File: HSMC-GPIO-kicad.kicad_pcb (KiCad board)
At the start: 2 copper layers, 63.5 x 78.1 mm, 107 parts, among them J1 HSMC, J2 Conn_01x03_Male, J3 I2C, J4 Screw_Terminal_01x04, J5 Conn_02x20_Odd_Even, U1 MC78M05_TO252, U2 TCA9517

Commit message: Reroute GPIO pins (again)
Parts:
- C18, C19, C2, C20, C3: footprint Capacitor_Tantalum_SMD:CP_EIA-3528-21_Kemet-B -> Capacitor_Tantalum_SMD:CP_EIA-3528-15_AVX-H
- moved J2 76.4 mm to (8.87, 35.1)
- moved C5 76.4 mm to (9.00, 38.2)
- moved C6 76.4 mm to (3.67, 38.2)
- moved J3 76.4 mm to (13.1, 42.7)
- moved U2 76.4 mm to (6.97, 40.2)
- moved C2 38.8 mm to (9.41, 59.1)
- moved C3 38.8 mm to (7.40, 71.6)
- moved C4 38.8 mm to (11.6, 73.1)
- moved U1 38.8 mm to (11.3, 65.5)
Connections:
- J1 pad 102: /GPIO20 -> /GPIO19
- J1 pad 104: /GPIO21 -> /GPIO18
- J1 pad 108: /GPIO22 -> /GPIO17
- J1 pad 110: /GPIO23 -> /GPIO16
- J1 pad 114: /GPIO24 -> /GPIO15
- J1 pad 116: /GPIO25 -> /GPIO14
- J1 pad 120: /GPIO26 -> /GPIO13
- J1 pad 122: /GPIO27 -> /GPIO12
- J1 pad 126: /GPIO28 -> /GPIO11
- J1 pad 128: /GPIO29 -> /GPIO10
- J1 pad 132: /GPIO30 -> /GPIO9
- J1 pad 134: /GPIO31 -> /GPIO8
- J1 pad 138: /GPIO32 -> /GPIO7
- J1 pad 140: /GPIO33 -> /GPIO6
- J1 pad 144: /GPIO34 -> /GPIO5
- J1 pad 146: /GPIO35 -> /GPIO4
- J1 pad 150: /GPIO36 -> /GPIO3
- J1 pad 152: /GPIO37 -> /GPIO2
- J1 pad 156: /GPIO38 -> /GPIO1
- J1 pad 158: /GPIO39 -> /GPIO0
- J1 pad 42: /GPIO0 -> /GPIO39
- J1 pad 44: /GPIO1 -> /GPIO38
- J1 pad 48: /GPIO2 -> /GPIO37
- J1 pad 50: /GPIO3 -> /GPIO36
- J1 pad 54: /GPIO4 -> /GPIO35
- J1 pad 56: /GPIO5 -> /GPIO34
- J1 pad 60: /GPIO6 -> /GPIO33
- J1 pad 62: /GPIO7 -> /GPIO32
- J1 pad 66: /GPIO8 -> /GPIO31
- J1 pad 68: /GPIO9 -> /GPIO30
- J1 pad 72: /GPIO10 -> /GPIO29
- J1 pad 74: /GPIO11 -> /GPIO28
- J1 pad 78: /GPIO12 -> /GPIO27
- J1 pad 80: /GPIO13 -> /GPIO26
- J1 pad 84: /GPIO14 -> /GPIO25
- J1 pad 86: /GPIO15 -> /GPIO24
- J1 pad 90: /GPIO16 -> /GPIO23
- J1 pad 92: /GPIO17 -> /GPIO22
- J1 pad 96: /GPIO18 -> /GPIO21
- J1 pad 98: /GPIO19 -> /GPIO20
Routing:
- net +5V: track 120.8 -> 8.95 mm
- net +3V3: track 225.2 -> 146.9 mm
- net +12V: track 118.8 -> 68.6 mm
- net /SDA: track 38.3 -> 1.50 mm
- net /SCL: track 32.8 -> 1.50 mm
- net /GPIO0: track 40.3 -> 33.9 mm
- net /GPIO1: track 40.1 -> 33.7 mm
- net /GPIO2: track 40.5 -> 34.3 mm
- net /GPIO3: track 39.7 -> 34.1 mm
- net /GPIO38: track 34.9 -> 40.0 mm
- net /GPIO4: track 39.9 -> 34.8 mm
- net /GPIO39: track 34.7 -> 39.8 mm
- net /GPIO37: track 34.4 -> 39.4 mm
- net /GPIO5: track 39.3 -> 34.6 mm
- net /GPIO7: track 39.2 -> 35.0 mm
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
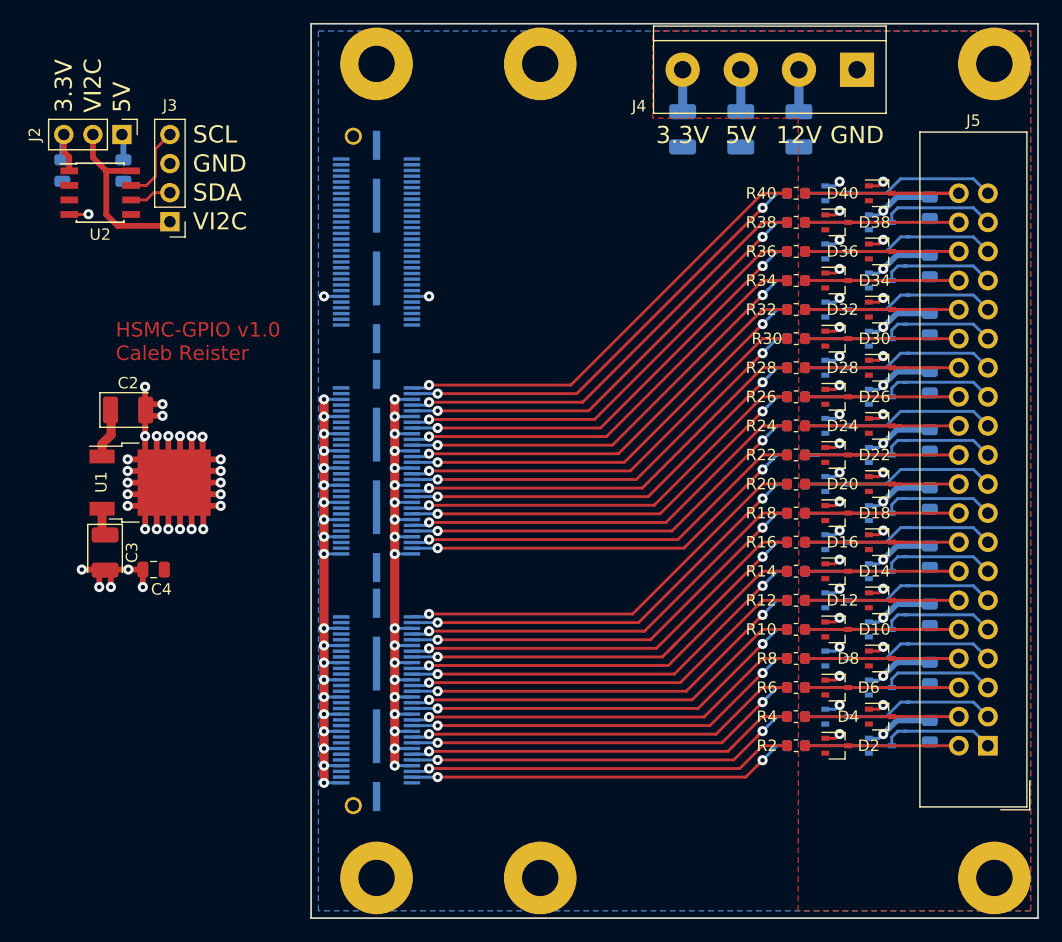
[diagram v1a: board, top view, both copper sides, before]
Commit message: Change BAT54S diode packages back to to SOT-23
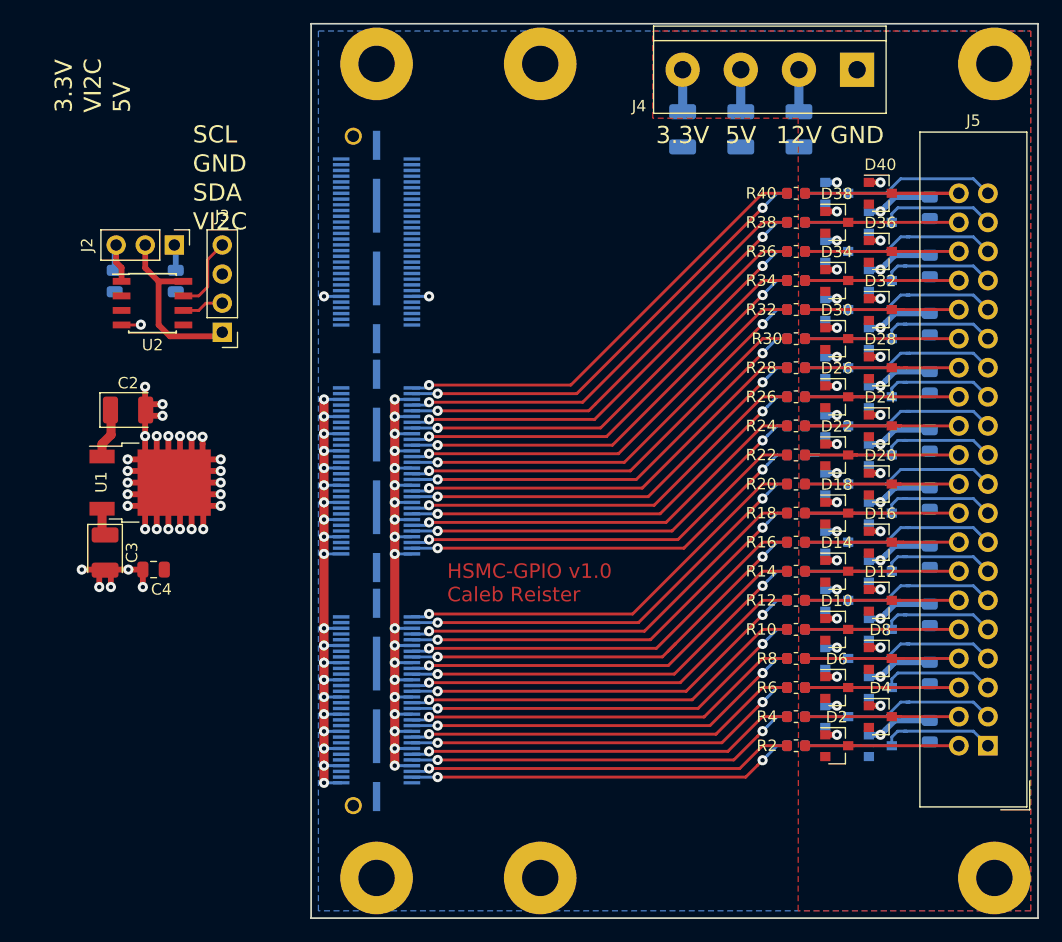
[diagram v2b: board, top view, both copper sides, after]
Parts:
- D1, D10, D11, D12, D13, D14, D15, D16, D17, D18, D19, D2, D20, D21, D22, D23, D24, D25, D26, D27, D28, D29, D3, D30, D31, D32, D33, D34, D35, D36, D37, D38, D39, D4, D40, D5, D6, D7, D8, D9: footprint Package_TO_SOT_SMD:SOT-323_SC-70 -> Package_TO_SOT_SMD:SOT-23
- moved C5 10.7 mm to (13.6, 47.9)
- moved C6 10.7 mm to (8.24, 47.9)
- moved J2 10.7 mm to (13.4, 44.7)
- moved J3 10.7 mm to (17.6, 52.3)
- moved U2 10.7 mm to (11.5, 49.8)
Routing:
- net GND: track 149.9 -> 142.1 mm
- net +3V3: track 146.9 -> 141.5 mm

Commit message: Fix issues and reroute I2C buffer, length match GPIO bus
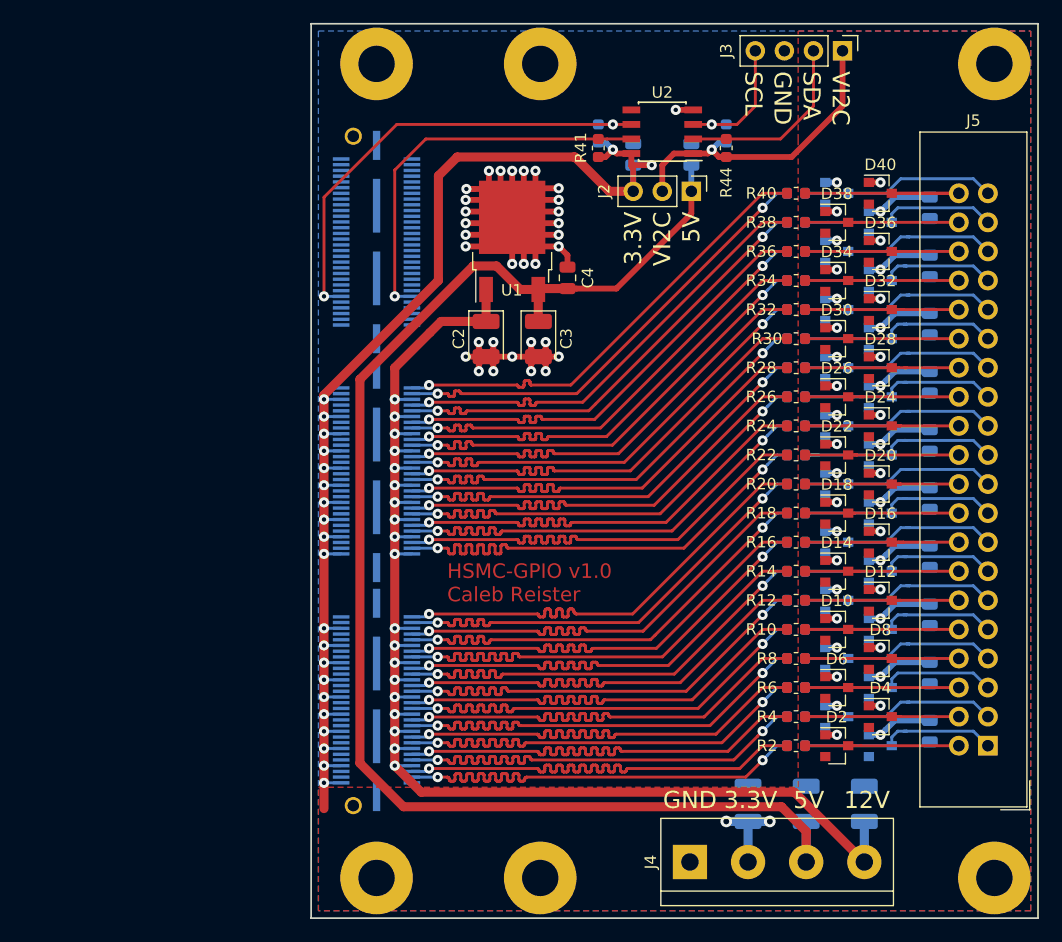
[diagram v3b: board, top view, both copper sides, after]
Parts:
- added R41: 10k, Resistor_SMD:R_0603_1608Metric, F.Cu at (50.5, 36.3)
- added R42: 10k, Resistor_SMD:R_0603_1608Metric, B.Cu at (50.5, 35.0)
- added R43: 2k, Resistor_SMD:R_0603_1608Metric, B.Cu at (61.7, 35.0)
- added R44: 2k, Resistor_SMD:R_0603_1608Metric, F.Cu at (61.7, 36.3)
- C18, C19, C2, C20, C3: footprint Capacitor_Tantalum_SMD:CP_EIA-3528-15_AVX-H -> Capacitor_Tantalum_SMD:CP_EIA-3528-21_Kemet-B
- U2: value TCA9517 -> PCA9507
- moved J4 70.7 mm to (58.5, 98.6), turned to 0 degrees
- moved J3 59.5 mm to (71.8, 27.8), turned to 270 degrees
- moved C18 59.2 mm to (68.6, 93.6), turned to 90 degrees
- moved C19 59.2 mm to (73.7, 93.6), turned to 90 degrees
- moved C20 59.2 mm to (63.6, 93.6), turned to 90 degrees
- moved U2 47.0 mm to (56.1, 34.8), turned to 180 degrees
- moved C6 46.6 mm to (53.5, 36.8), turned to 270 degrees
- moved C5 46.4 mm to (58.6, 36.8), turned to 270 degrees
- moved J2 45.4 mm to (58.6, 40.0)
- moved C4 44.2 mm to (47.8, 47.6), turned to 270 degrees
- moved C3 42.2 mm to (45.3, 52.9)
- moved U1 38.0 mm to (43.0, 44.4), turned to 90 degrees
- moved C2 31.9 mm to (40.7, 52.9), turned to 270 degrees
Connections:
- J2 pad 2: /VI2C -> VBUS
- J3 pad 1: /VI2C -> VBUS
- J4 pad 2: +12V -> +3V3
- J4 pad 4: +3V3 -> +12V
- U2 pad 1: +3V3 -> VBUS
- U2 pad 2: /SCL -> Net-(J3-Pad2)
- U2 pad 3: /SDA -> Net-(J3-Pad4)
- U2 pad 6: Net-(J3-Pad2) -> /SDA
- U2 pad 7: Net-(J3-Pad4) -> /SCL
- U2 pad 8: /VI2C -> +3V3
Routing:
- net +5V: track 8.95 -> 124.9 mm
- net +3V3: track 141.5 -> 197.9 mm, vias 40 -> 44
- net +12V: track 68.6 -> 123.8 mm
- net /SDA: track 1.50 -> 40.9 mm, vias 1 -> 2
- net /SCL: track 1.50 -> 34.3 mm
- net VBUS: track 0.00 -> 27.1 mm, vias 0 -> 1
- net /VI2C: track 15.9 -> 0.00 mm
- net Net-(J3-Pad2): track 3.66 -> 16.5 mm
- net /GPIO1: track 33.7 -> 40.7 mm
- net /GPIO20: track 36.1 -> 42.9 mm
- net /GPIO0: track 33.9 -> 40.6 mm
- net /GPIO3: track 34.1 -> 40.7 mm
- net /GPIO2: track 34.3 -> 40.7 mm
- net /GPIO5: track 34.6 -> 40.7 mm
- net /GPIO4: track 34.8 -> 40.7 mm
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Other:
- net class Power: via_dia 1.016 -> 0.889; via_drill 0.508 -> 0.381

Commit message: Rotate GPIO connector 180deg, reroute
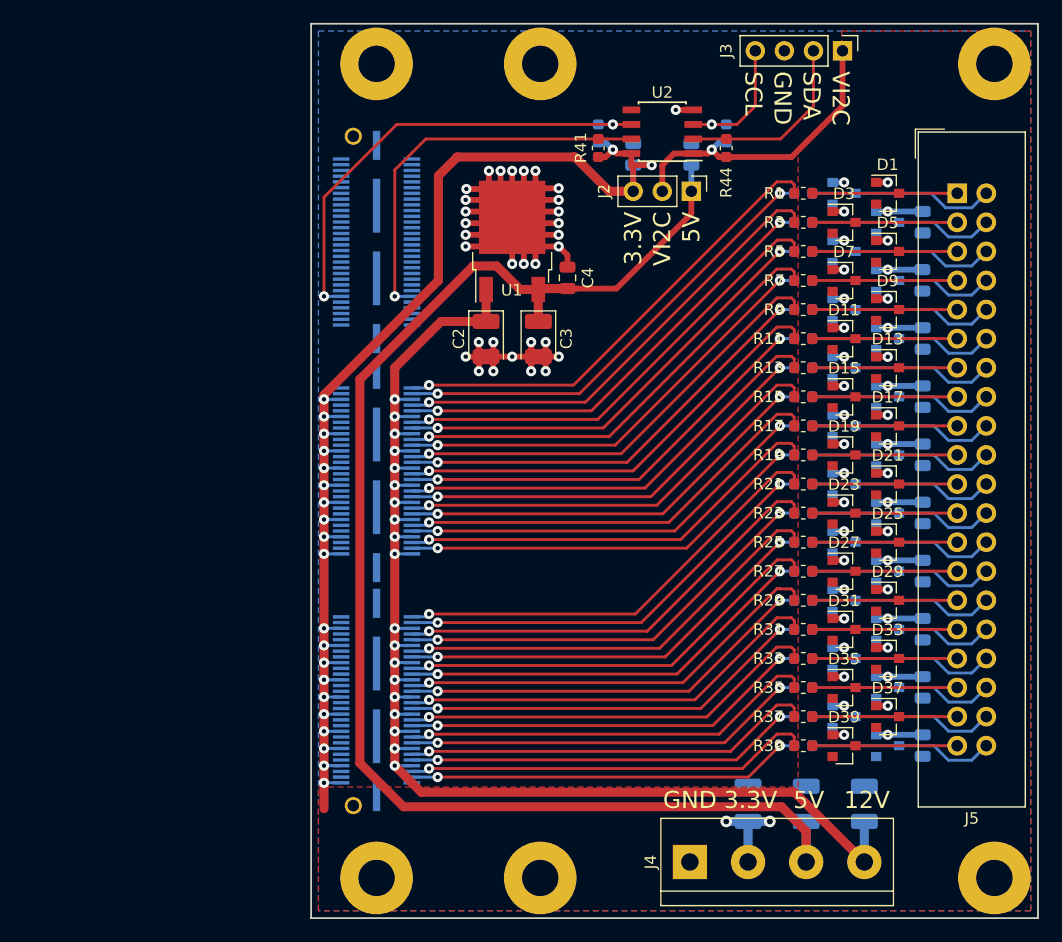
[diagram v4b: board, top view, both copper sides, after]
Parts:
- D1, D11, D13, D15, D17, D19, D21, D23, D25, D27, D29, D3, D31, D33, D35, D37, D39, D5, D7, D9, R1, R11, R13, R15, R17, R19, R21, R23, R25, R27, R29, R3, R31, R33, R35, R37, R39, R5, R7, R9: moved to F.Cu
- D10, D12, D14, D16, D18, D2, D20, D22, D24, D26, D28, D30, D32, D34, D36, D38, D4, D40, D6, D8, R10, R12, R14, R16, R18, R2, R20, R22, R24, R26, R28, R30, R32, R34, R36, R38, R4, R40, R6, R8: moved to B.Cu
- moved J5 48.3 mm to (81.8, 40.2), turned to 0 degrees
- moved D1 48.3 mm to (75.8, 40.2)
- moved D2 48.3 mm to (72.0, 40.2)
- moved D39 48.3 mm to (72.0, 88.5)
- moved D40 48.3 mm to (75.8, 88.5)
- moved R1 48.3 mm to (68.4, 40.2)
- moved R2 48.3 mm to (68.4, 40.2)
- moved R39 48.3 mm to (68.4, 88.5)
- moved R40 48.3 mm to (68.4, 88.5)
- moved D3 43.2 mm to (72.0, 42.8)
- moved D37 43.2 mm to (75.8, 85.9)
- moved D38 43.2 mm to (72.0, 85.9)
- moved D4 43.2 mm to (75.8, 42.8)
- moved R3 43.2 mm to (68.4, 42.8)
- moved R37 43.2 mm to (68.4, 85.9)
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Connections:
- J1 pad 102: /GPIO19 -> /GPIO20
- J1 pad 104: /GPIO18 -> /GPIO21
- J1 pad 108: /GPIO17 -> /GPIO22
- J1 pad 110: /GPIO16 -> /GPIO23
- J1 pad 114: /GPIO15 -> /GPIO24
- J1 pad 116: /GPIO14 -> /GPIO25
- J1 pad 120: /GPIO13 -> /GPIO26
- J1 pad 122: /GPIO12 -> /GPIO27
- J1 pad 126: /GPIO11 -> /GPIO28
- J1 pad 128: /GPIO10 -> /GPIO29
- J1 pad 132: /GPIO9 -> /GPIO30
- J1 pad 134: /GPIO8 -> /GPIO31
- J1 pad 138: /GPIO7 -> /GPIO32
- J1 pad 140: /GPIO6 -> /GPIO33
- J1 pad 144: /GPIO5 -> /GPIO34
- J1 pad 146: /GPIO4 -> /GPIO35
- J1 pad 150: /GPIO3 -> /GPIO36
- J1 pad 152: /GPIO2 -> /GPIO37
- J1 pad 156: /GPIO1 -> /GPIO38
- J1 pad 158: /GPIO0 -> /GPIO39
- J1 pad 42: /GPIO39 -> /GPIO0
- J1 pad 44: /GPIO38 -> /GPIO1
- J1 pad 48: /GPIO37 -> /GPIO2
- J1 pad 50: /GPIO36 -> /GPIO3
- J1 pad 54: /GPIO35 -> /GPIO4
- J1 pad 56: /GPIO34 -> /GPIO5
- J1 pad 60: /GPIO33 -> /GPIO6
- J1 pad 62: /GPIO32 -> /GPIO7
- J1 pad 66: /GPIO31 -> /GPIO8
- J1 pad 68: /GPIO30 -> /GPIO9
- J1 pad 72: /GPIO29 -> /GPIO10
- J1 pad 74: /GPIO28 -> /GPIO11
- J1 pad 78: /GPIO27 -> /GPIO12
- J1 pad 80: /GPIO26 -> /GPIO13
- J1 pad 84: /GPIO25 -> /GPIO14
- J1 pad 86: /GPIO24 -> /GPIO15
- J1 pad 90: /GPIO23 -> /GPIO16
- J1 pad 92: /GPIO22 -> /GPIO17
- J1 pad 96: /GPIO21 -> /GPIO18
- J1 pad 98: /GPIO20 -> /GPIO19
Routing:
- net +3V3: track 197.9 -> 183.0 mm
- net /GPIO/P5: track 22.0 -> 12.7 mm
- net /GPIO/P9: track 21.5 -> 12.7 mm
- net /GPIO39: track 40.7 -> 34.5 mm, vias 1 -> 2
- net /GPIO/P21: track 18.7 -> 12.7 mm
- net /GPIO37: track 40.6 -> 35.0 mm, vias 1 -> 2
- net /GPIO/P1: track 18.2 -> 12.7 mm
- net /GPIO/P13: track 17.9 -> 12.7 mm
- net /GPIO/P29: track 17.9 -> 12.7 mm
- net /GPIO35: track 40.6 -> 35.4 mm, vias 1 -> 2
- net /GPIO/P25: track 17.7 -> 12.7 mm
- net /GPIO/P33: track 17.7 -> 12.7 mm
- net /GPIO/P17: track 17.7 -> 12.7 mm
- net /GPIO/P37: track 17.7 -> 12.7 mm
- net /GPIO38: track 40.7 -> 35.6 mm, vias 2 -> 1
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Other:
- board text removed: "HSMC-GPIO v1.0 Caleb Reister"
